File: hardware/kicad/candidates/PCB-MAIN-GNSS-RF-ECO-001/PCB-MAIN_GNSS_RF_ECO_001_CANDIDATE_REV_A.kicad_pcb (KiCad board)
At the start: 6 copper layers, 110 x 75 mm, 251 parts, among them J10 U.FL-R-SMT-1(60), J11 USB4105-GF-A-120, J12 MEM2052-00-195-00-A, J13 504050-0291, J6 2336582-1, J7 2336582-1, J8 U.FL-R-SMT-1(60), J9 U.FL-R-SMT-1(60), Q1 MMBT3904,215, Q2 MMBT3904,215, Q3 MMBT3904,215, Q4 Si1016X-T1-GE3, U1 STM32U585VIT6Q, U10 E22-900M22S, U11 MDBT50Q-P1MV2, U13 TS3A27518EPWR, U14 ESDALC6V1-5P6, U15 ESDALC6V1-5P6, U16 SN74AXC8T245PWR, U17 SN74LVC32APWR, U18 SN74AXC1T45DRLR, U19 TPD4E05U06DQAR, U2 W25Q512JVFIQ, U20 TPD4E05U06DQAR, U21 TPD4E05U06DQAR, U22 TPD4E05U06DQAR, U23 TPD4E05U06DQAR, U24 TPD4E05U06DQAR, U25 TPD2EUSB30DRTR, U26 TPD2EUSB30DRTR, U27 TPD4E05U06DQAR, U3 LIS2DW12TR, U4 STTS22HTR, U5 LT6000IDCB#TRMPBF, U6 SN74LVC1G07DBVR, U7 SN74AXC8T245PWR, U8 BG95-M3, U9 MAX-M10S-00B, X1 SiT1552AI-JE-DCC-32.768D

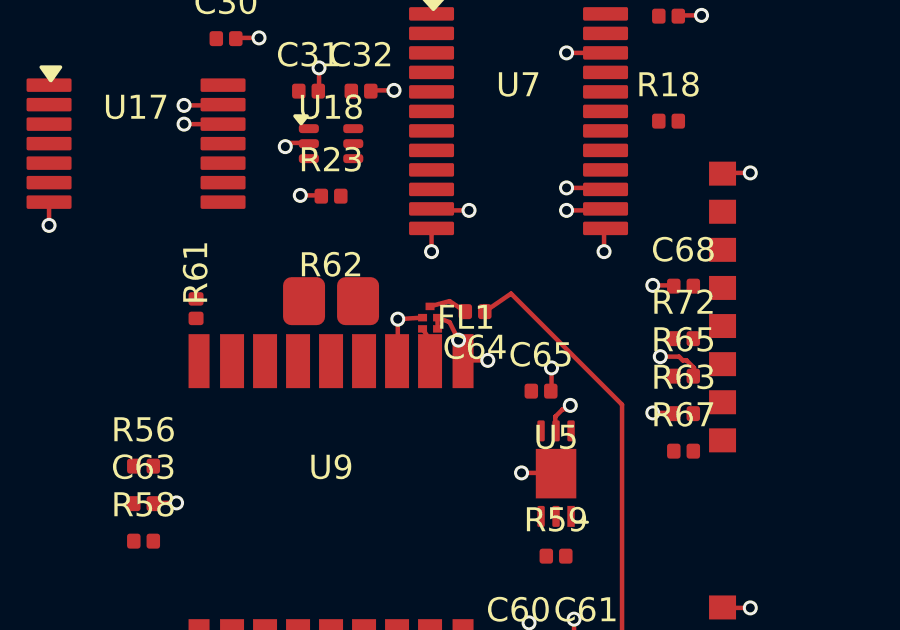
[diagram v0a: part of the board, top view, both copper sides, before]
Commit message: hardware: increase GNSS filter ground clearance
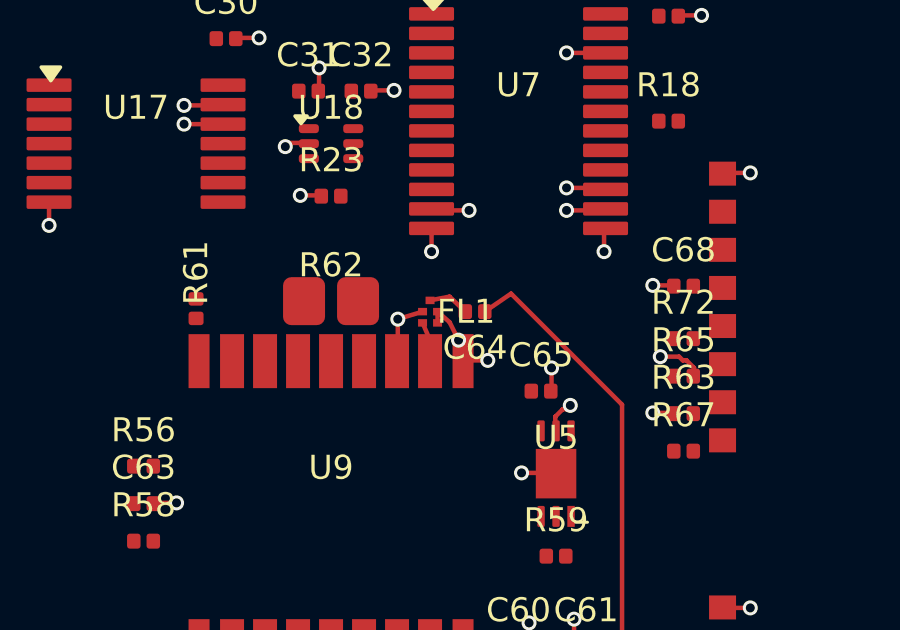
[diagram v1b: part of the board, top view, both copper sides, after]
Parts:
- moved FL1 0.20 mm to (56.8, 51.6)
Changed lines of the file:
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@@
   )
   (footprint "Abracon_ABSES5AF_1109-5" (layer "F.Cu")
-    (at 56.8 51.8 270)
+    (at 56.8 51.6 270)
     (descr "Abracon ABSES5AF-L100KM 1.1x0.9 mm 5-pad SAW; datasheet 2025-09-16 recommended land pattern")
     (tags "Abracon ABSES5AF SAW 1109-5 GNSS")
@@
   (segment (start 63.2 54.7) (end 59.5 51) (width 0.1509) (layer "F.Cu") (net 57))
   (segment (start 59.5 51) (end 58.625 51.6) (width 0.1509) (layer "F.Cu") (net 57))
-  (segment (start 57.975 51.6) (end 57.45 51.25) (width 0.1509) (layer "F.Cu") (net 58))
-  (segment (start 57.45 51.25) (end 56.8 51.425) (width 0.1509) (layer "F.Cu") (net 58))
+  (segment (start 57.975 51.6) (end 57.45 51.1) (width 0.1509) (layer "F.Cu") (net 58))
+  (segment (start 57.45 51.1) (end 56.8 51.225) (width 0.1509) (layer "F.Cu") (net 58))
   (segment (start 56.8 53.25) (end 56.8 52.55) (width 0.1509) (layer "F.Cu") (net 59))
-  (segment (start 56.8 52.55) (end 56.55 52.175) (width 0.1509) (layer "F.Cu") (net 59))
-  (segment (start 56.55 51.8) (end 55.725 51.85) (width 0.15) (layer "F.Cu") (net 45))
-  (segment (start 57.05 52.175) (end 57.05 51.8) (width 0.15) (layer "F.Cu") (net 45))
-  (segment (start 57.05 51.8) (end 57.45 51.95) (width 0.15) (layer "F.Cu") (net 45))
+  (segment (start 56.8 52.55) (end 56.55 51.975) (width 0.1509) (layer "F.Cu") (net 59))
+  (segment (start 56.55 51.6) (end 55.725 51.85) (width 0.15) (layer "F.Cu") (net 45))
+  (segment (start 57.05 51.975) (end 57.05 51.6) (width 0.15) (layer "F.Cu") (net 45))
+  (segment (start 57.05 51.6) (end 57.45 51.95) (width 0.15) (layer "F.Cu") (net 45))
   (segment (start 57.45 51.95) (end 57.75 52.55) (width 0.15) (layer "F.Cu") (net 45))
   (via (at 57.75 52.55) (size 0.5) (drill 0.3) (layers "F.Cu" "B.Cu") (net 45))
